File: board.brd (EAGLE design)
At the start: 50 x 50 mm, 32 parts

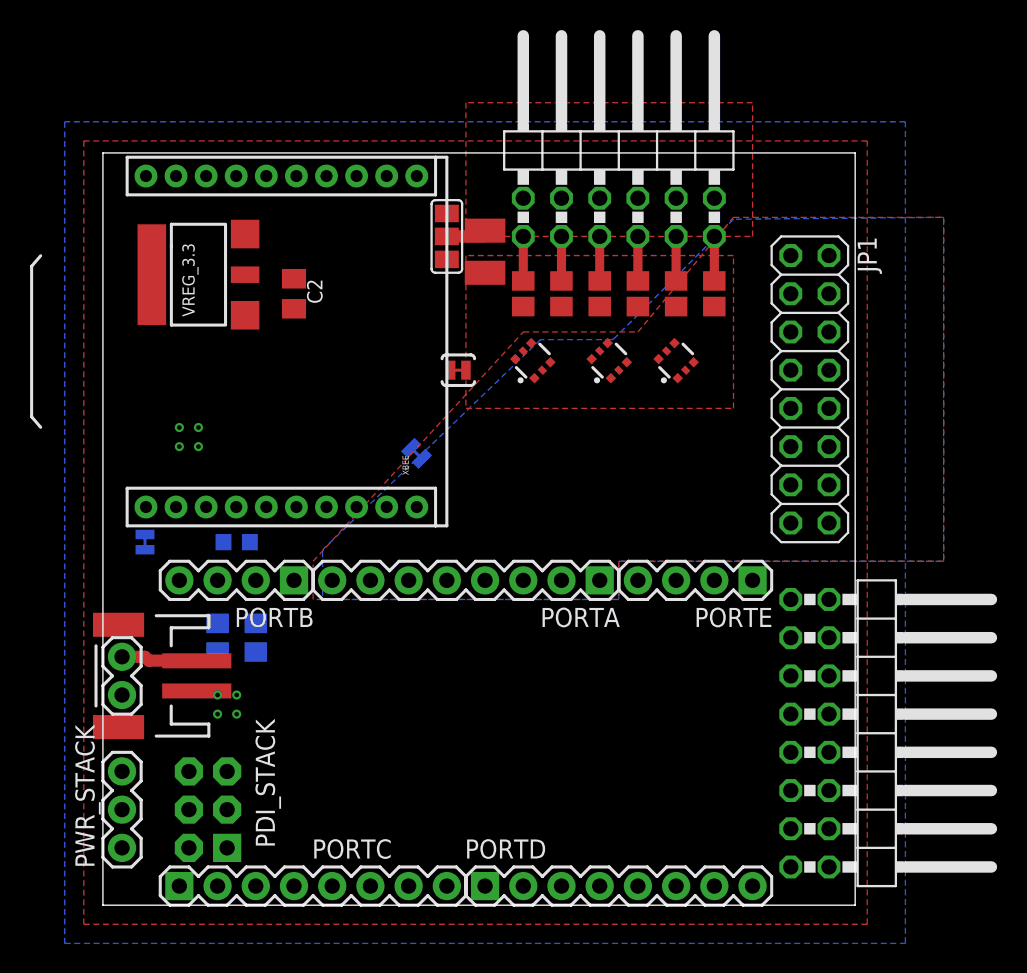
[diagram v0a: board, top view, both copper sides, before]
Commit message: routed, not very nice or optimal I guess, but it should work
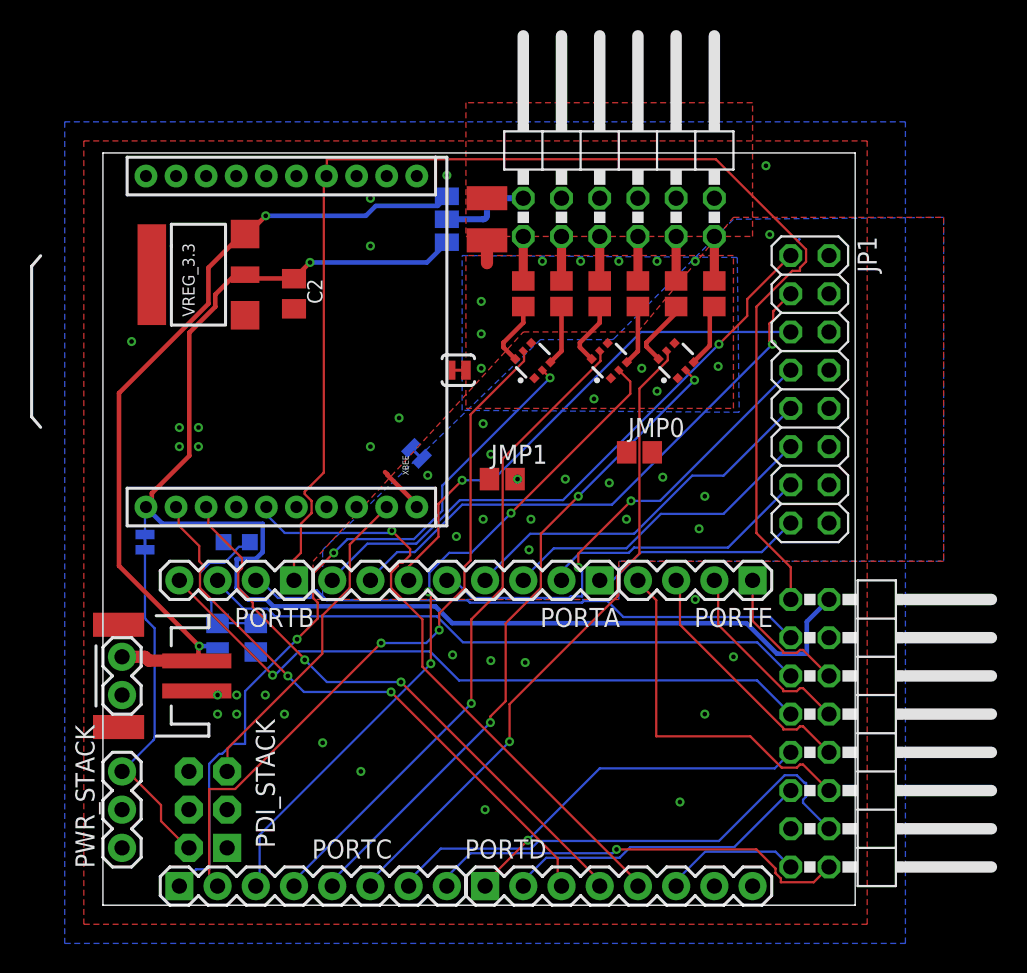
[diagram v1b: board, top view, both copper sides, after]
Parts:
- added JMP0, JMP1: (no value), resistor:R0805
- moved C3 2.16 mm to (25.5, 45.6)
- moved SJ2 1.14 mm to (22.9, 45.6), flipped to the bottom
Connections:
- net AGND: now also JMP0.1, JMP0.2, JMP1.1, JMP1.2
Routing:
- net +3V3: track 0.00 -> 93.0 mm, vias 0 -> 1
- net PB0/XMEGA_AREF: track 0.00 -> 89.5 mm
- net VBAT: track 5.35 -> 55.5 mm, vias 0 -> 2
- net PWM0: track 0.00 -> 48.7 mm, vias 0 -> 3
- net PWM1: track 0.00 -> 47.3 mm, vias 0 -> 2
- net PWM2: track 0.00 -> 46.1 mm, vias 0 -> 3
- net PB3: track 0.00 -> 45.7 mm, vias 0 -> 1
- net PWM4: track 0.00 -> 44.5 mm, vias 0 -> 3
- net PWM3: track 0.00 -> 44.0 mm, vias 0 -> 1
- net PWM5: track 0.00 -> 43.8 mm, vias 0 -> 1
- net XBEE_RESET: track 0.00 -> 41.1 mm, vias 0 -> 1
- net PB2: track 0.00 -> 40.8 mm
- net PA7: track 0.00 -> 40.1 mm, vias 0 -> 1
- net XMEGA_RX0: track 0.00 -> 39.4 mm, vias 0 -> 2
- net XMEGA_TX0: track 0.00 -> 39.1 mm, vias 0 -> 2
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- added copper zone on layer 16, net PGND

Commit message: mark the jumper resistor values
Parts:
- JMP0, JMP1: value (none) -> 0R
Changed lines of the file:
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@@
 <element name="+3.3V_VXMEGA" library="SparkFun-Passives" package="SJ_2S-TRACE" value="SOLDERJUMPERTRACE" x="2.794" y="24.13" smashed="yes" rot="MR270"/>
 <element name="C2" library="rcl" package="C0805K" value="" x="12.7" y="40.64" rot="R270"/>
-<element name="JMP0" library="resistor" package="R0805" value="" x="35.6616" y="30.099"/>
-<element name="JMP1" library="resistor" package="R0805" value="" x="26.543" y="28.321"/>
+<element name="JMP0" library="resistor" package="R0805" value="0R" x="35.6616" y="30.099"/>
+<element name="JMP1" library="resistor" package="R0805" value="0R" x="26.543" y="28.321"/>
 </elements>
 <signals>

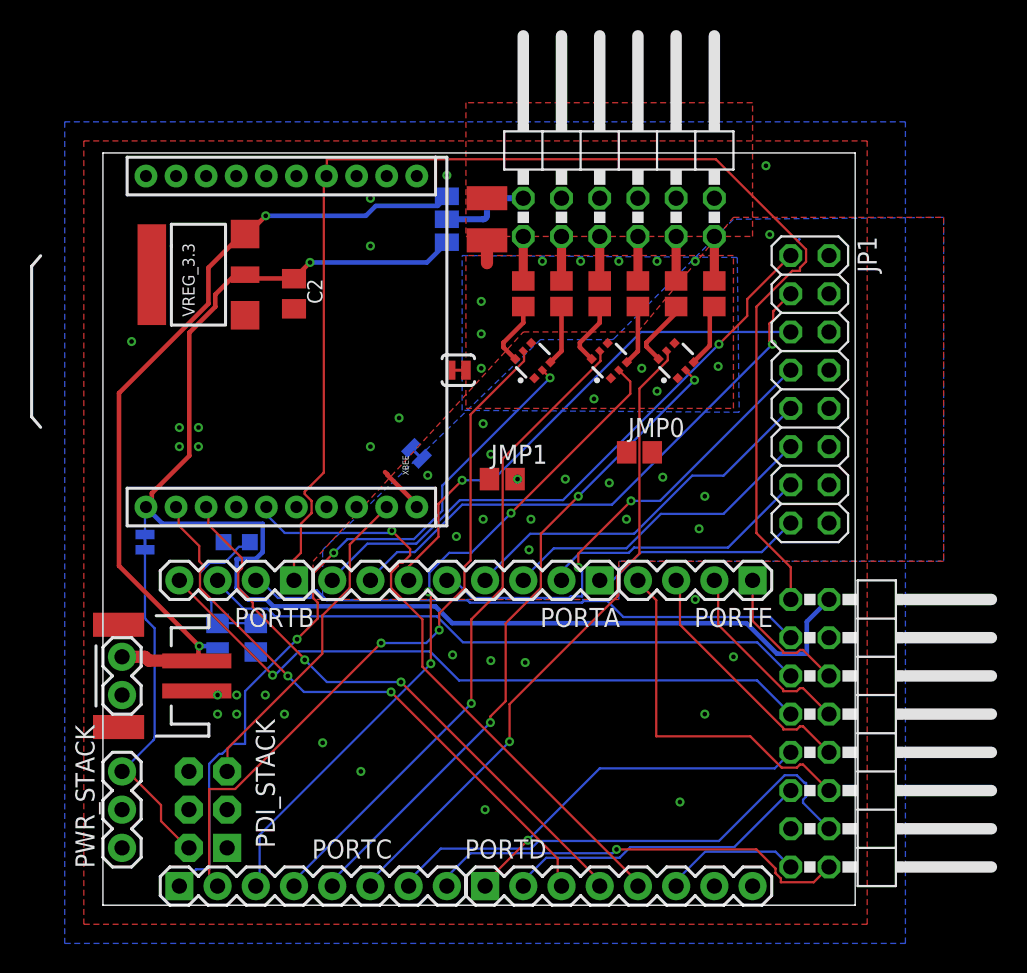
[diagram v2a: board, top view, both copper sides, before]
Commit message: freeroute.net base routing and adjustments + gnd vias on top
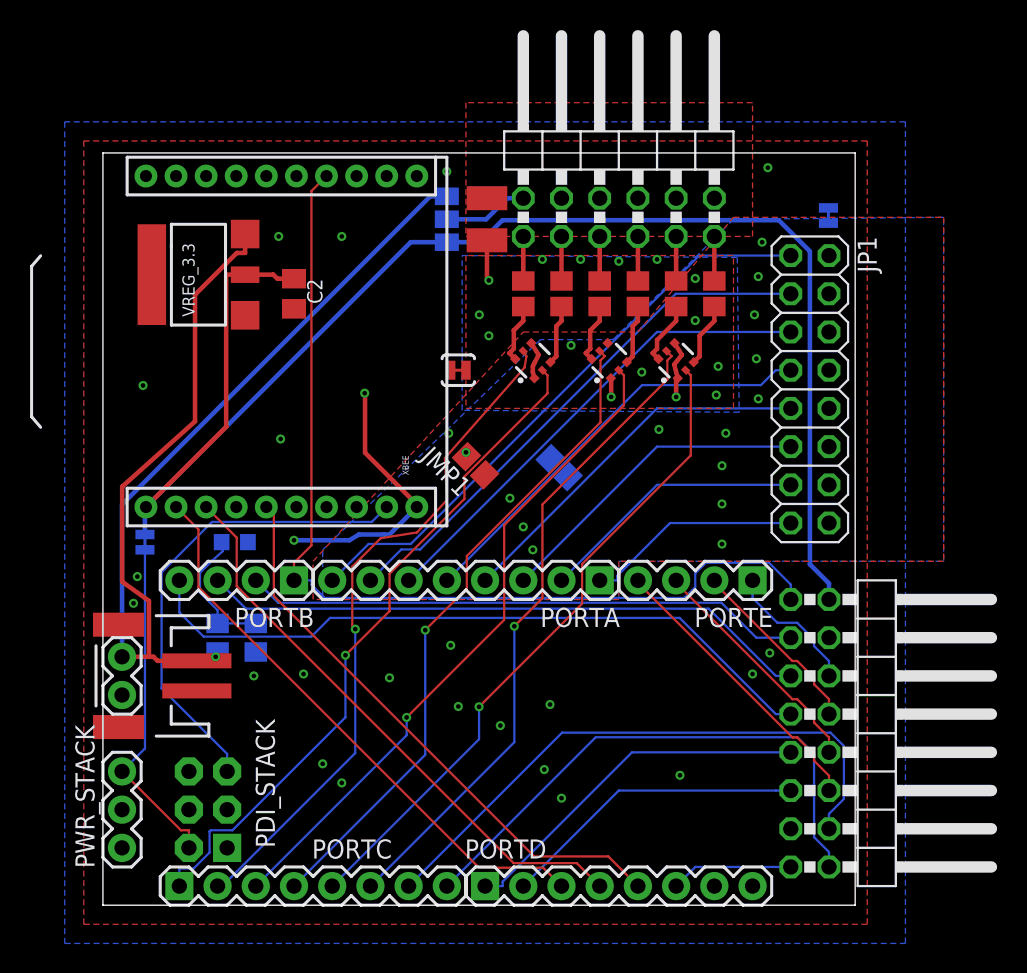
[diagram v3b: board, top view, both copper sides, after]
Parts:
- moved AGND_GND 31.6 mm to (48.2, 45.8), turned to 90 degrees
- moved JMP0 5.43 mm to (30.3, 29.1), flipped to the bottom, turned to 45 degrees
- moved JMP1 1.99 mm to (24.8, 29.2), turned to 135 degrees
- moved C1 0.13 mm to (8.76, 24.1), turned to 180 degrees
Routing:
- net PB0/XMEGA_AREF: track 89.5 -> 64.5 mm
- net VBAT: track 55.5 -> 80.1 mm, vias 2 -> 1
- net GND: track 3.25 -> 18.1 mm, vias 27 -> 24
- net PDI_RESET/CLK: track 22.0 -> 31.8 mm
- net PGND: track 1.52 -> 10.4 mm, vias 12 -> 15
- net XMEGA_TX1: track 28.4 -> 36.9 mm, vias 1 -> 0
- net +3V3: track 93.0 -> 100.7 mm, vias 1 -> 0
- net XMEGA_RX1: track 33.7 -> 39.4 mm
- net PE3: track 24.0 -> 19.4 mm
- net PA4: track 31.6 -> 28.6 mm, vias 2 -> 0
- net XBEE_RESET: track 41.1 -> 38.3 mm, vias 1 -> 0
- net PWM0: track 48.7 -> 46.0 mm, vias 3 -> 1
- net PWM1: track 47.3 -> 45.3 mm, vias 2 -> 1
- net PA5: track 34.1 -> 32.2 mm, vias 1 -> 0
- net VBAT_SENSE: track 10.9 -> 9.18 mm
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
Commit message: get rid of agnd
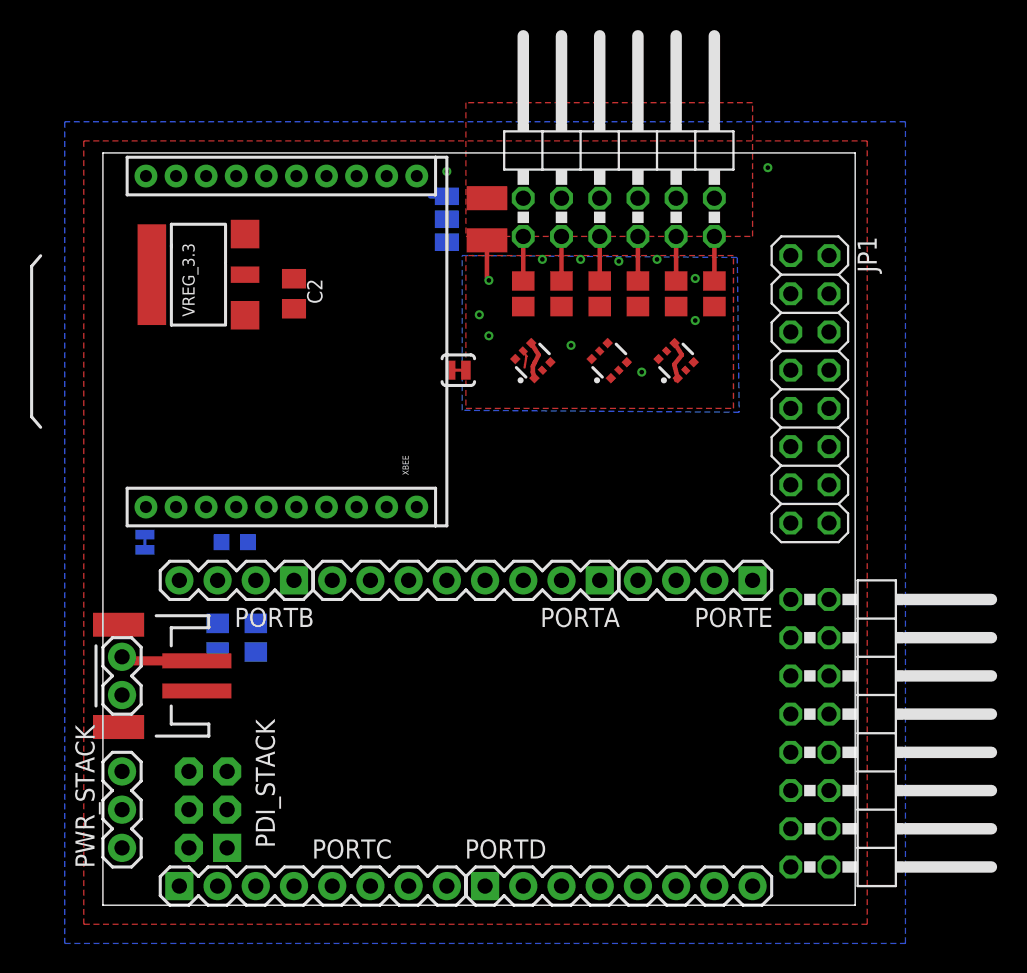
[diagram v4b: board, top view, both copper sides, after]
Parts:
- removed AGND_GND: SOLDERJUMPERTRACE, SparkFun-Passives:SJ_2S-TRACE
- removed JMP0, JMP1: 0R, resistor:R0805
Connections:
- removed net AGND: AGND_GND.1, JMP0.1, JMP0.2, JMP1.1, JMP1.2, JP1.10, JP1.12, JP1.14, JP1.16, JP1.2, JP1.4, JP1.6, JP1.8
- net GND: now also JP1.10, JP1.12, JP1.14, JP1.16, JP1.2, JP1.4, JP1.6, JP1.8; no longer AGND_GND.2
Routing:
- net +3V3: track 100.7 -> 0.00 mm
- net VBAT: track 80.1 -> 6.35 mm, vias 1 -> 0
- net PB0/XMEGA_AREF: track 64.5 -> 0.00 mm
- net PB3: track 46.6 -> 0.00 mm
- net PWM0: track 46.0 -> 0.00 mm, vias 1 -> 0
- net PWM2: track 44.6 -> 0.00 mm, vias 1 -> 0
- net PWM4: track 44.3 -> 0.00 mm, vias 1 -> 0
- net PWM3: track 44.3 -> 0.00 mm, vias 1 -> 0
- net PWM1: track 45.3 -> 1.17 mm, vias 1 -> 0
- net PWM5: track 44.0 -> 0.00 mm, vias 1 -> 0
- net PB2: track 40.7 -> 0.00 mm
- net XMEGA_RX1: track 39.4 -> 0.00 mm
- net PA7: track 39.4 -> 0.00 mm
- net XMEGA_TX0: track 38.5 -> 0.00 mm
- net XBEE_RESET: track 38.3 -> 0.00 mm
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- removed copper zone on layer 1, net AGND
- removed copper zone on layer 16, net AGND

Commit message: the xbee aref is not used on series2 anyway
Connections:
- net GND: now also XBEE.14
- net PB0/XMEGA_AREF: no longer XBEE.14
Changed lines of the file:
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@@
 <contactref element="JP1" pad="12"/>
 <contactref element="JP1" pad="14"/>
+<contactref element="XBEE" pad="14"/>
 </signal>
 <signal name="PDI_DATA">
@@
 <signal name="PB0/XMEGA_AREF">
 <contactref element="PORTB" pad="1"/>
-<contactref element="XBEE" pad="14"/>
 <contactref element="JP2" pad="1"/>
 <wire x1="12.7" y1="21.59" x2="45.72" y2="20.32" width="0" layer="19" extent="1-1"/>
-<wire x1="14.86" y1="48.465" x2="12.7" y2="21.59" width="0" layer="19" extent="1-1"/>
 </signal>
 <signal name="XBEE_RESET">

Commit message: adjust some vias
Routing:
- net PGND: vias 11 -> 6
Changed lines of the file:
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@@
 </polygon>
 <wire x1="25.527" y1="41.5883" x2="25.527" y2="44.193" width="0.3048" layer="1"/>
-<via x="36.83" y="42.926" extent="1-16" drill="0.3048" diameter="0.6096"/>
+<via x="36.83" y="42.799" extent="1-16" drill="0.3048" diameter="0.6096"/>
 <via x="34.29" y="42.799" extent="1-16" drill="0.3048" diameter="0.6096"/>
-<via x="31.75" y="42.926" extent="1-16" drill="0.3048" diameter="0.6096"/>
-<via x="29.21" y="42.926" extent="1-16" drill="0.3048" diameter="0.6096"/>
+<via x="31.75" y="42.799" extent="1-16" drill="0.3048" diameter="0.6096"/>
+<via x="29.21" y="42.799" extent="1-16" drill="0.3048" diameter="0.6096"/>
 <via x="25.654" y="41.529" extent="1-16" drill="0.3048" diameter="0.6096"/>
-<via x="25.019" y="39.243" extent="1-16" drill="0.3048" diameter="0.6096"/>
-<via x="25.654" y="37.846" extent="1-16" drill="0.3048" diameter="0.6096"/>
-<via x="31.115" y="37.211" extent="1-16" drill="0.3048" diameter="0.6096"/>
-<via x="35.814" y="35.433" extent="1-16" drill="0.3048" diameter="0.6096"/>
-<via x="39.37" y="38.862" extent="1-16" drill="0.3048" diameter="0.6096"/>
-<via x="39.37" y="41.656" extent="1-16" drill="0.3048" diameter="0.6096"/>
+<via x="39.37" y="42.799" extent="1-16" drill="0.3048" diameter="0.6096"/>
 <wire x1="38.1" y1="34.8996" x2="38.2016" y2="35.0012" width="0.3048" layer="1"/>
 <wire x1="38.2016" y1="35.0012" x2="38.206065625" y2="35.028271875" width="0.3048" layer="1"/>

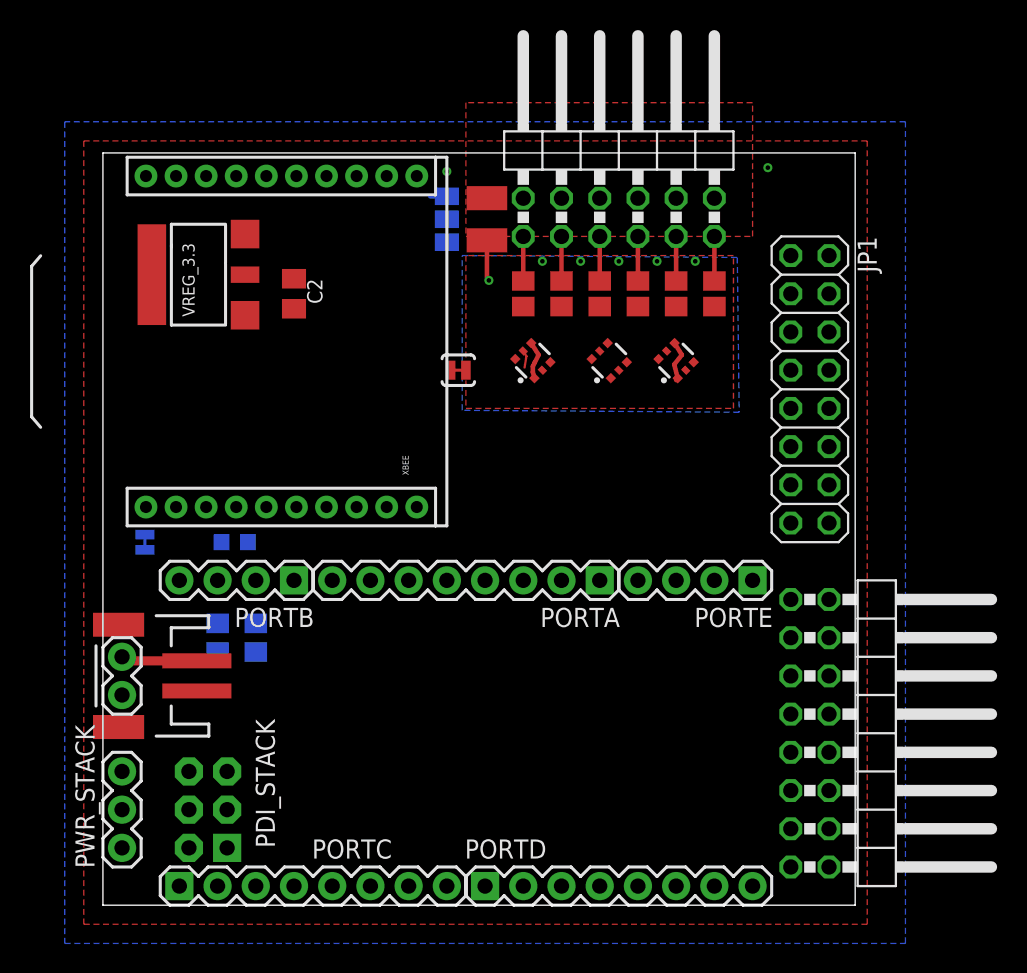
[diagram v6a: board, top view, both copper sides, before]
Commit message: version without agnd (but needs no jumper-resistors), the lipo-charger is still missing
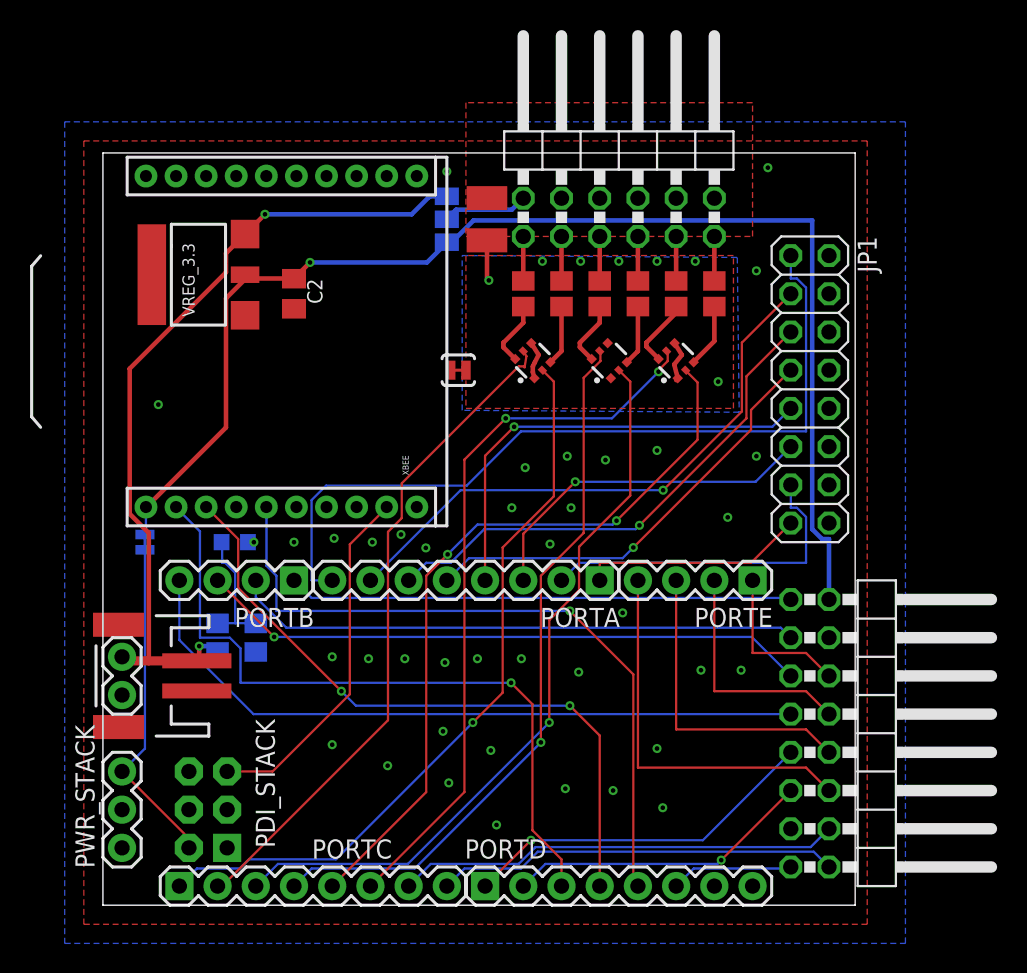
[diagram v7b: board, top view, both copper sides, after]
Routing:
- net +3V3: track 0.00 -> 85.6 mm, vias 0 -> 1
- net PA7: track 0.00 -> 53.8 mm
- net PWM2: track 0.00 -> 50.0 mm, vias 0 -> 1
- net PWM0: track 0.00 -> 50.0 mm, vias 0 -> 1
- net PWM4: track 0.00 -> 49.9 mm, vias 0 -> 2
- net PWM3: track 0.00 -> 48.0 mm, vias 0 -> 1
- net PWM5: track 0.00 -> 47.9 mm, vias 0 -> 2
- net VBAT: track 6.35 -> 54.2 mm, vias 0 -> 2
- net XMEGA_RX0: track 0.00 -> 47.5 mm, vias 0 -> 1
- net XBEE_RESET: track 0.00 -> 46.8 mm, vias 0 -> 1
- net PB3: track 0.00 -> 46.6 mm
- net XMEGA_TX0: track 0.00 -> 44.4 mm, vias 0 -> 2
- net PWM1: track 1.17 -> 44.6 mm
- net PB2: track 0.00 -> 40.7 mm, vias 0 -> 1
- net PA6: track 0.00 -> 38.5 mm, vias 0 -> 1
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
